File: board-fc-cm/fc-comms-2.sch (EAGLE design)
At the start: 228 parts, among them IC1 TPS79930QDDCRQ1, IC10 FM25V10, IC11 MPU-9250, IC12 TXB0108PW, IC13 TPS3813K33-EP_DBV_6, IC14 TMP100-EP_DBV_6, IC15 LHA1+, IC16 PCT2075TP, IC17 MMZ09332BT1, IC18 PCT2075TP, IC2 TPS79930QDDCRQ1, IC3 MSP430FR2311PW, IC4 MCP1700TT, IC5 TXB0108PW, IC6 TXB0108PW, IC7 CC1125RHBT, IC77 74LVC1G08, IC8 CC1125RHBT, IC9 TM4C123[7,G]XXPM, J3 SWD_SHROUD, Q3 32.768kHz, Q4 BSS123, Q5 BSS84, X1 SHIELD-26X26, X2 SHIELD-26X26, X3 LFTCXO070, X4 LFTCXO070, X5 SHIELD-26X26, X6 SHIELD-26X26, Y1 8MHz

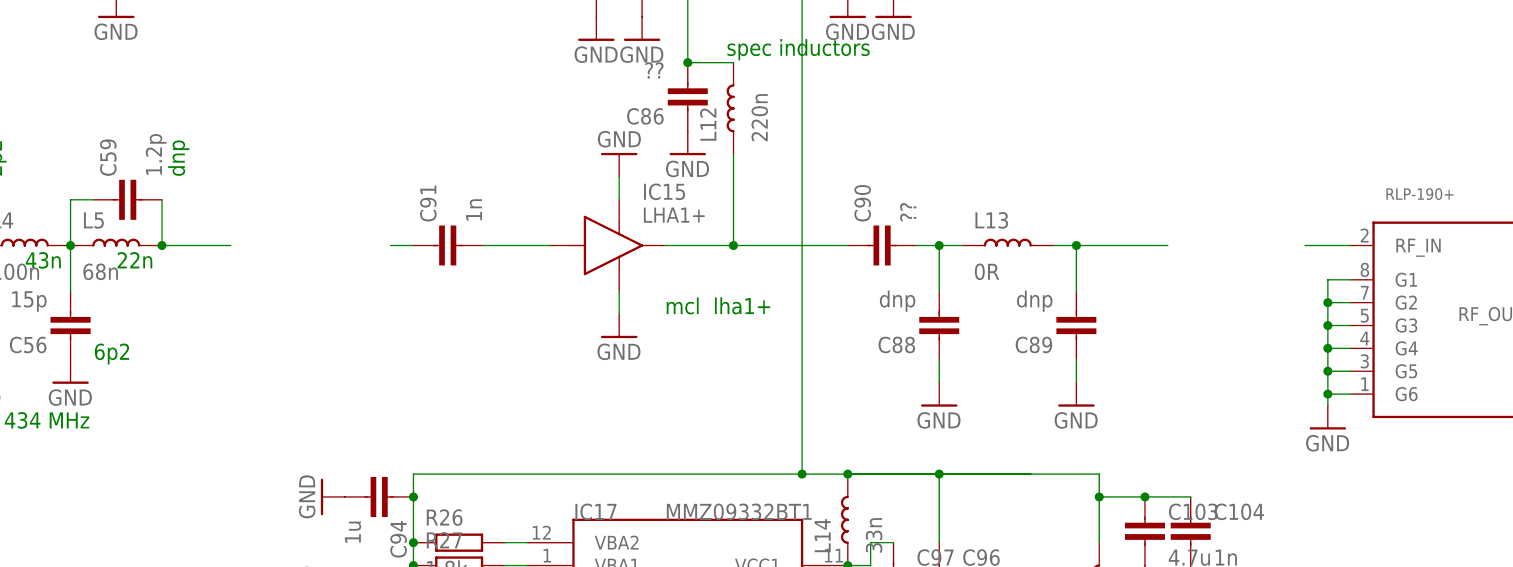
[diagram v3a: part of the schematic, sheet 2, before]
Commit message: switching to lha1+, camera rx/tx done
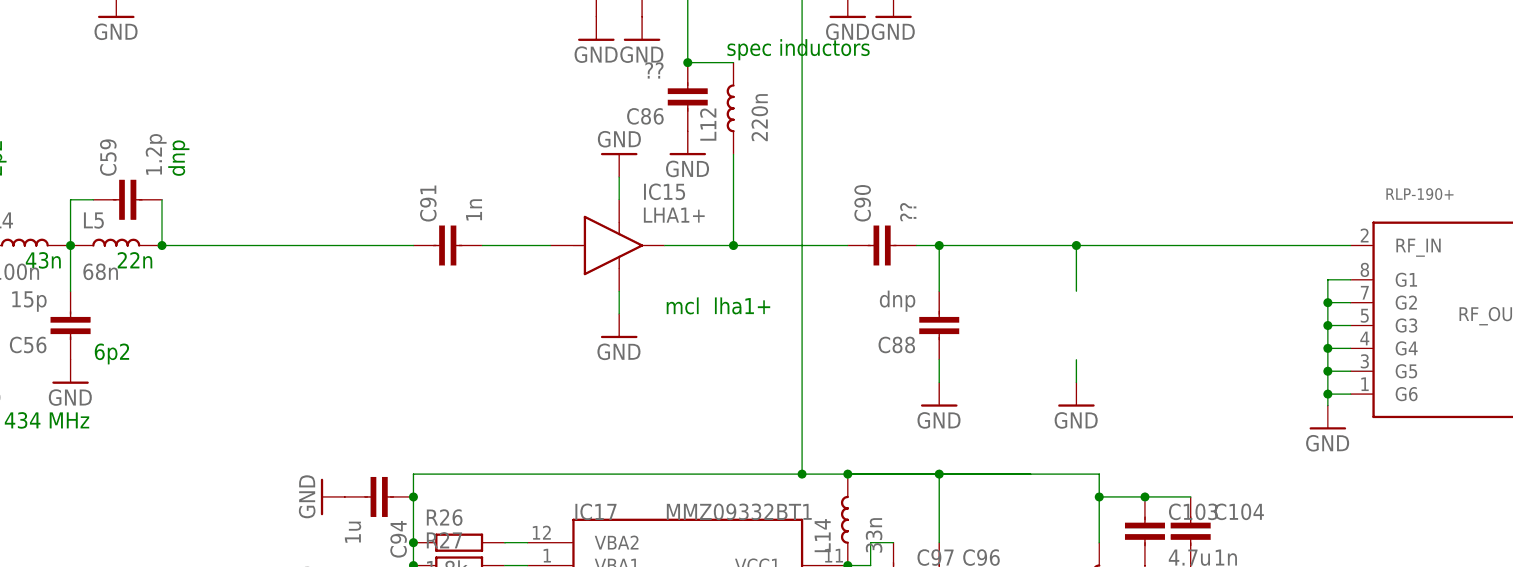
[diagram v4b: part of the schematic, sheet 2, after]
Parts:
- removed C89: dnp, passives-7351:CAPACITOR0603-N
- removed L13: 0R, passives-7351:INDUCTOR0603-N
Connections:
- removed net N$28: FL3.RF_IN
- removed net N$37: C89.2, L13.P$2
- new net N$24: JP7.3, R18.P$1
- net GND: no longer C89.1
- net N$23: now also C91.1
- net N$26: now also JP7.4, R17.P$1; no longer C91.1
- net N$27: now also FL3.RF_IN; no longer L13.P$1
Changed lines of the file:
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@@
 <part name="C86" library="passives-7351" deviceset="CAPACITOR" device="0603-N" value="??"/>
 <part name="GND26" library="supply1" deviceset="GND" device=""/>
-<part name="L13" library="passives-7351" deviceset="INDUCTOR" device="0603-N" value="0R"/>
 <part name="C88" library="passives-7351" deviceset="CAPACITOR" device="0603-N" value="dnp"/>
 <part name="GND28" library="supply1" deviceset="GND" device=""/>
@@
 <part name="C57" library="passives-7351" deviceset="CAPACITOR" device="0603-N" value="5.1p"/>
 <part name="L7" library="passives-7351" deviceset="INDUCTOR" device="0603-N" value="27u"/>
-<part name="C89" library="passives-7351" deviceset="CAPACITOR" device="0603-N" value="dnp"/>
 <part name="FL2" library="CubeSat3" deviceset="SAW_FILTER_CS" device=""/>
 <part name="GND57" library="supply1" deviceset="GND" device=""/>
@@
 </segment>
 </net>
+<net name="N$24" class="0">
+<segment>
+<pinref part="R18" gate="G$1" pin="P$1"/>
+<wire x1="401.32" y1="223.52" x2="408.94" y2="223.52" width="0.1524" layer="91"/>
+<wire x1="408.94" y1="223.52" x2="411.48" y2="226.06" width="0.1524" layer="91"/>
+<pinref part="JP7" gate="G$1" pin="3"/>
+<wire x1="411.48" y1="226.06" x2="426.72" y2="226.06" width="0.1524" layer="91"/>
+</segment>
+</net>
+<net name="N$26" class="0">
+<segment>
+<pinref part="JP7" gate="G$1" pin="4"/>
+<wire x1="426.72" y1="223.52" x2="411.48" y2="223.52" width="0.1524" layer="91"/>
+<wire x1="411.48" y1="223.52" x2="408.94" y2="226.06" width="0.1524" layer="91"/>
+<pinref part="R17" gate="G$1" pin="P$1"/>
+<wire x1="408.94" y1="226.06" x2="401.32" y2="226.06" width="0.1524" layer="91"/>
+</segment>
+</net>
 </nets>
 </sheet>
@@
 <instance part="C86" gate="G$1" x="208.28" y="66.04" rot="R180"/>
 <instance part="GND26" gate="1" x="208.28" y="60.96"/>
-<instance part="L13" gate="G$1" x="243.84" y="50.8"/>
 <instance part="C88" gate="G$1" x="236.22" y="40.64" rot="R180"/>
 <instance part="GND28" gate="1" x="251.46" y="33.02"/>
@@
 <instance part="C57" gate="G$1" x="137.16" y="-154.94" rot="R90"/>
 <instance part="L7" gate="G$1" x="139.7" y="-137.16"/>
-<instance part="C89" gate="G$1" x="251.46" y="40.64" rot="R180"/>
 <instance part="FL2" gate="G$1" x="266.7" y="-152.4" rot="MR0"/>
 <instance part="GND57" gate="1" x="292.1" y="-144.78" rot="MR0"/>
@@
 </segment>
 <segment>
-<pinref part="C89" gate="G$1" pin="1"/>
 <pinref part="GND28" gate="1" pin="GND"/>
 <wire x1="251.46" y1="38.1" x2="251.46" y2="35.56" width="0.1524" layer="91"/>
@@
 <pinref part="L5" gate="G$1" pin="P$2"/>
 <wire x1="149.86" y1="55.88" x2="149.86" y2="50.8" width="0.1524" layer="91"/>
-<wire x1="149.86" y1="50.8" x2="157.48" y2="50.8" width="0.1524" layer="91"/>
 <junction x="149.86" y="50.8"/>
+<pinref part="C91" gate="G$1" pin="1"/>
+<wire x1="149.86" y1="50.8" x2="177.8" y2="50.8" width="0.1524" layer="91"/>
 </segment>
 </net>
@@
 <pinref part="C90" gate="G$1" pin="1"/>
 <junction x="213.36" y="50.8"/>
-</segment>
-</net>
-<net name="N$26" class="0">
-<segment>
-<pinref part="C91" gate="G$1" pin="1"/>
-<wire x1="175.26" y1="50.8" x2="177.8" y2="50.8" width="0.1524" layer="91"/>
-</segment>
-</net>
-<net name="N$28" class="0">
-<segment>
-<pinref part="FL3" gate="G$1" pin="RF_IN"/>
-<wire x1="281.94" y1="50.8" x2="276.86" y2="50.8" width="0.1524" layer="91"/>
 </segment>
 </net>
@@
 <segment>
 <pinref part="C90" gate="G$1" pin="2"/>
-<pinref part="L13" gate="G$1" pin="P$1"/>
 <wire x1="233.68" y1="50.8" x2="236.22" y2="50.8" width="0.1524" layer="91"/>
 <pinref part="C88" gate="G$1" pin="2"/>
-<wire x1="236.22" y1="50.8" x2="238.76" y2="50.8" width="0.1524" layer="91"/>
 <wire x1="236.22" y1="45.72" x2="236.22" y2="50.8" width="0.1524" layer="91"/>
 <junction x="236.22" y="50.8"/>
-</segment>
-</net>
-<net name="N$37" class="0">
-<segment>
-<pinref part="L13" gate="G$1" pin="P$2"/>
-<wire x1="248.92" y1="50.8" x2="251.46" y2="50.8" width="0.1524" layer="91"/>
-<pinref part="C89" gate="G$1" pin="2"/>
-<wire x1="251.46" y1="50.8" x2="261.62" y2="50.8" width="0.1524" layer="91"/>
 <wire x1="251.46" y1="45.72" x2="251.46" y2="50.8" width="0.1524" layer="91"/>
 <junction x="251.46" y="50.8"/>
-</segment>
-</net>
+<pinref part="FL3" gate="G$1" pin="RF_IN"/>
+<wire x1="251.46" y1="50.8" x2="281.94" y2="50.8" width="0.1524" layer="91"/>
+<wire x1="236.22" y1="50.8" x2="251.46" y2="50.8" width="0.1524" layer="91"/>
+</segment>
+</net>
